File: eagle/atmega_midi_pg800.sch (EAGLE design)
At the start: 36 parts, among them IC1 78L05Z, IC2 4067N, IC3 4067N, IC4 4067N, Q1 16.000Mhz, U1 6N138, U2 ATMEGA328P_PDIP, X1 MAB6H

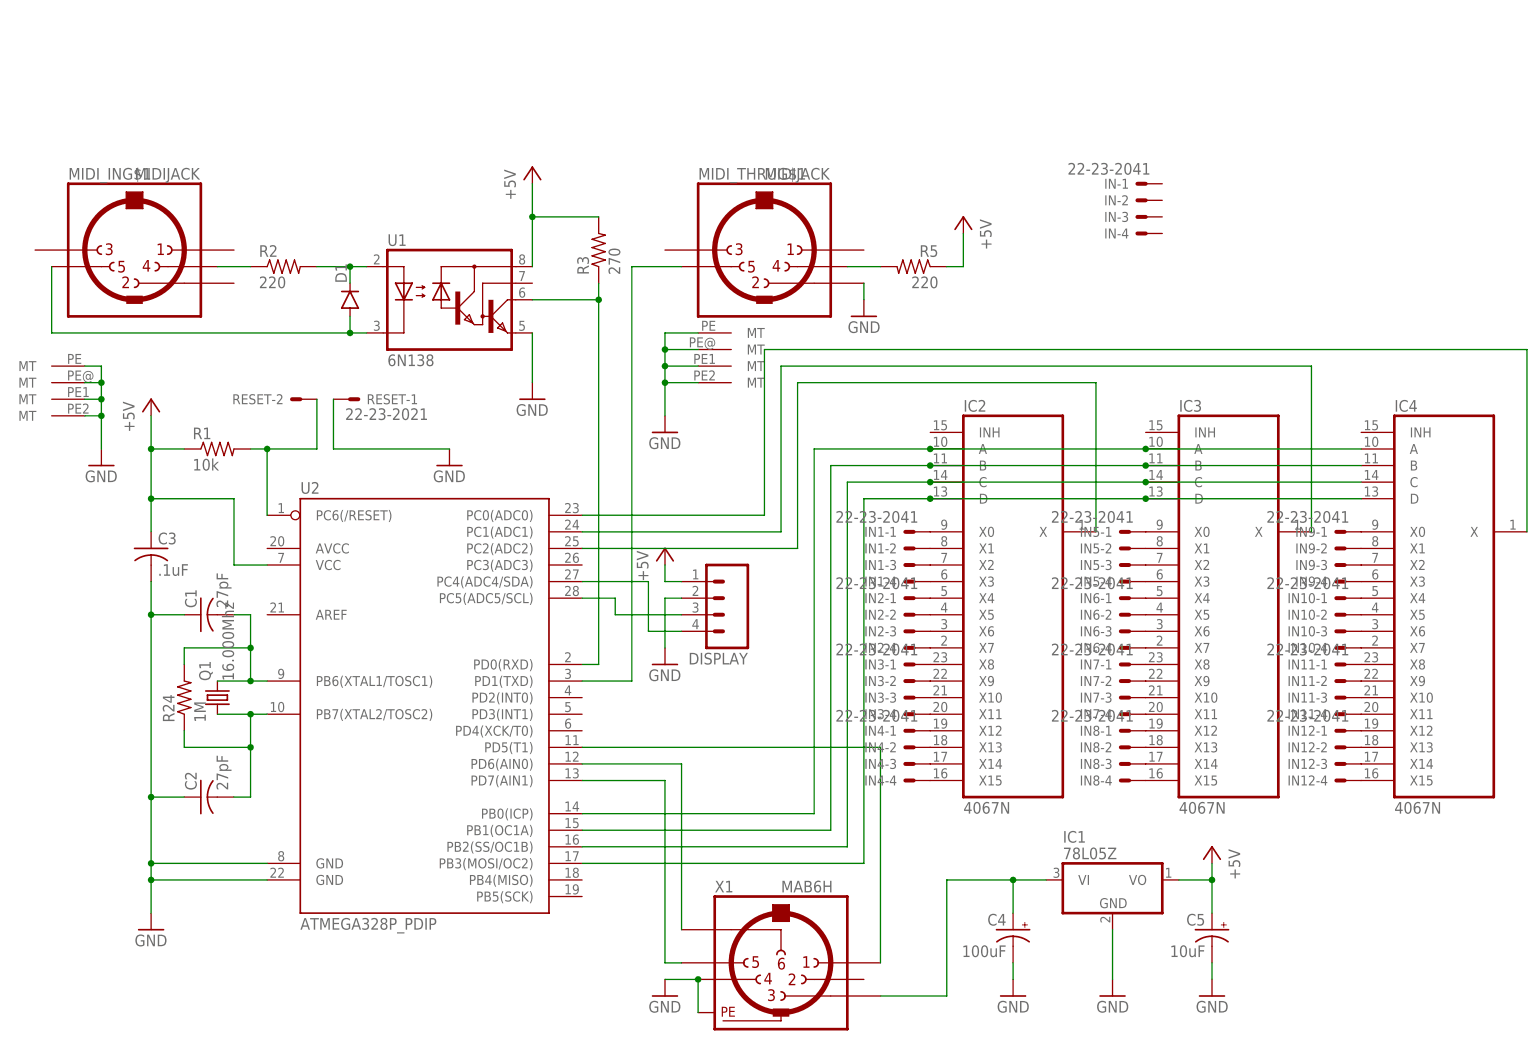
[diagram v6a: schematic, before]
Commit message: placement improved
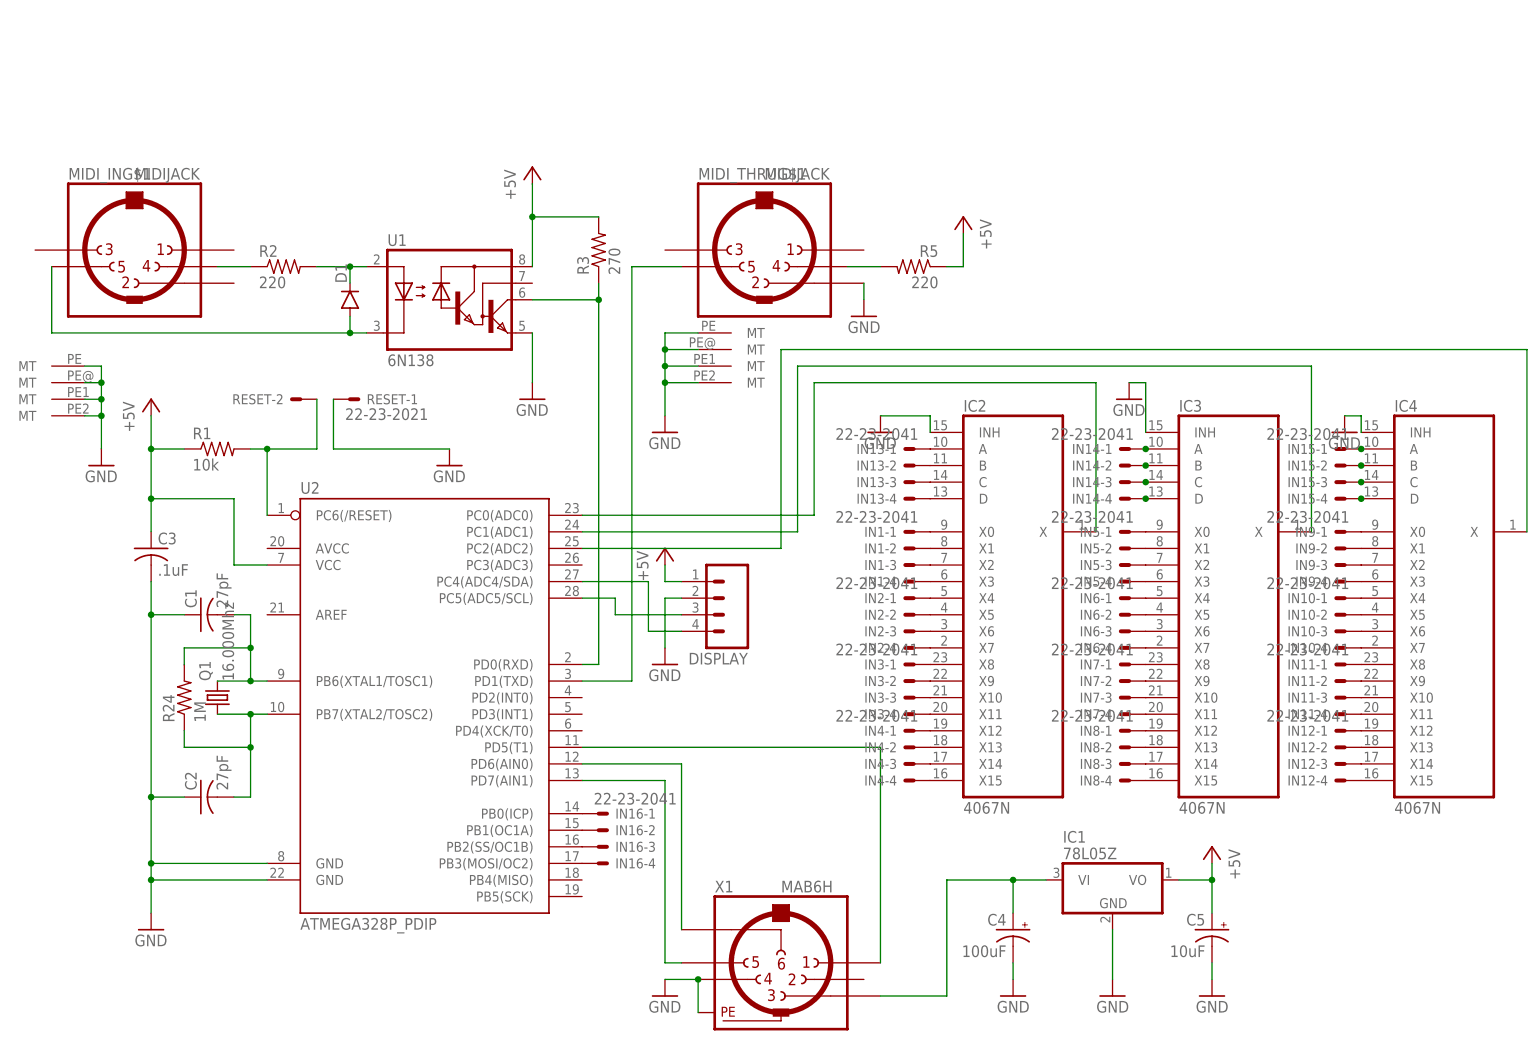
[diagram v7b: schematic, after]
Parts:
- removed IN: 22-23-2041, con-molex:22-23-2041
- added IN13, IN14, IN15, IN16: 22-23-2041, con-molex:22-23-2041
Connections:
- new net N$71: IC3A.C, IN14-3.S
- new net N$72: IC3A.D, IN14-4.S
- new net N$73: IC4A.A, IN15-1.S
- new net N$74: IC4A.B, IN15-2.S
- new net N$75: IC4A.C, IN15-3.S
- new net N$76: IC4A.D, IN15-4.S
- new net N$77: IN16-3.S, U2.PB2(SS/OC1B)
- new net N$78: IN16-4.S, U2.PB3(MOSI/OC2)
- new net N$80: IC2A.D, IN13-4.S
- new net N$81: IC2A.C, IN13-3.S
- new net N$82: IC2A.B, IN13-2.S
- new net N$83: IC2A.A, IN13-1.S
- net GND: now also IC2A.INH, IC3A.INH, IC4A.INH
- net N$15: now also U2.PC0(ADC0); no longer U2.PC2(ADC2)
- net N$16: now also IN16-1.S; no longer IC2A.A, IC3A.A, IC4A.A
- net N$17: now also IN16-2.S; no longer IC2A.B, IC3A.B, IC4A.B
- net N$18: now also IC3A.A, IN14-1.S; no longer IC2A.C, IC3A.C, IC4A.C, U2.PB2(SS/OC1B)
- net N$19: now also IC3A.B, IN14-2.S; no longer IC2A.D, IC3A.D, IC4A.D, U2.PB3(MOSI/OC2)
- net N$2: now also U2.PC2(ADC2); no longer U2.PC0(ADC0)

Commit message: standard connector for display
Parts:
- DISPLAY: value (none) -> 22-23-2041; device SparkFun-Connectors:M04POLAR -> con-molex:22-23-2041
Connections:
- net +5V: now also DISPLAY-4.S; no longer DISPLAY.1
- net GND: now also DISPLAY-3.S; no longer DISPLAY.2
- net N$12: now also DISPLAY-2.S; no longer DISPLAY.3
- net N$13: now also DISPLAY-1.S; no longer DISPLAY.4
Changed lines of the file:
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@@
 <?xml version="1.0" encoding="utf-8"?>
 <!DOCTYPE eagle SYSTEM "eagle.dtd">
-<eagle version="7.7.0">
+<eagle version="7.6.0">
 <drawing>
 <settings>
@@
 <part name="GND6" library="supply1" deviceset="GND" device=""/>
 <part name="RESET" library="con-molex" deviceset="22-23-2021" device=""/>
-<part name="DISPLAY" library="SparkFun-Connectors" deviceset="M04" device="POLAR"/>
 <part name="P+5" library="supply1" deviceset="+5V" device=""/>
 <part name="GND7" library="supply1" deviceset="GND" device=""/>
@@
 <part name="GND11" library="supply1" deviceset="GND" device=""/>
 <part name="IN16" library="con-molex" deviceset="22-23-2041" device=""/>
+<part name="DISPLAY" library="con-molex" deviceset="22-23-2041" device=""/>
 </parts>
 <sheets>
@@
 <instance part="RESET" gate="-1" x="5.08" y="91.44" rot="MR180"/>
 <instance part="RESET" gate="-2" x="-2.54" y="91.44" rot="MR0"/>
-<instance part="DISPLAY" gate="G$1" x="60.96" y="60.96" rot="R180"/>
 <instance part="P+5" gate="1" x="53.34" y="68.58"/>
 <instance part="GND7" gate="1" x="53.34" y="50.8"/>
@@
 <instance part="IN16" gate="-3" x="43.18" y="22.86"/>
 <instance part="IN16" gate="-4" x="43.18" y="20.32"/>
+<instance part="DISPLAY" gate="-1" x="58.42" y="55.88" rot="MR180"/>
+<instance part="DISPLAY" gate="-2" x="58.42" y="58.42" rot="MR180"/>
+<instance part="DISPLAY" gate="-3" x="58.42" y="60.96" rot="MR180"/>
+<instance part="DISPLAY" gate="-4" x="58.42" y="63.5" rot="MR180"/>
 </instances>
 <busses>
@@
 </segment>
 <segment>
-<pinref part="DISPLAY" gate="G$1" pin="1"/>
 <pinref part="P+5" gate="1" pin="+5V"/>
 <wire x1="53.34" y1="66.04" x2="53.34" y2="63.5" width="0.1524" layer="91"/>
 <wire x1="53.34" y1="63.5" x2="55.88" y2="63.5" width="0.1524" layer="91"/>
+<pinref part="DISPLAY" gate="-4" pin="S"/>
 </segment>
 </net>
@@
 </segment>
 <segment>
-<pinref part="DISPLAY" gate="G$1" pin="2"/>
 <pinref part="GND7" gate="1" pin="GND"/>
+<wire x1="53.34" y1="60.96" x2="53.34" y2="53.34" width="0.1524" layer="91"/>
+<pinref part="DISPLAY" gate="-3" pin="S"/>
 <wire x1="55.88" y1="60.96" x2="53.34" y2="60.96" width="0.1524" layer="91"/>
-<wire x1="53.34" y1="60.96" x2="53.34" y2="53.34" width="0.1524" layer="91"/>
 </segment>
 <segment>
@@
 <wire x1="45.72" y1="60.96" x2="45.72" y2="58.42" width="0.1524" layer="91"/>
 <wire x1="45.72" y1="58.42" x2="55.88" y2="58.42" width="0.1524" layer="91"/>
-<pinref part="DISPLAY" gate="G$1" pin="3"/>
 <pinref part="U2" gate="G$1" pin="PC5(ADC5/SCL)"/>
+<pinref part="DISPLAY" gate="-2" pin="S"/>
 </segment>
 </net>
 <net name="N$13" class="0">
 <segment>
-<pinref part="DISPLAY" gate="G$1" pin="4"/>
 <wire x1="55.88" y1="55.88" x2="50.8" y2="55.88" width="0.1524" layer="91"/>
 <wire x1="50.8" y1="55.88" x2="50.8" y2="63.5" width="0.1524" layer="91"/>
 <wire x1="50.8" y1="63.5" x2="40.64" y2="63.5" width="0.1524" layer="91"/>
 <pinref part="U2" gate="G$1" pin="PC4(ADC4/SDA)"/>
-</segment>
-</net>
+<pinref part="DISPLAY" gate="-1" pin="S"/>
+</segment>
+</net>
